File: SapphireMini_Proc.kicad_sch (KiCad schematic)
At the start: 64 parts, among them J801 USB_B_Micro, J802 Conn_02x05_Odd_Even, J803 Conn_02x05_Odd_Even, J805 Conn_01x04_Male, SW801 EVQP7C01P, U801 ATSAMD21G18A-A

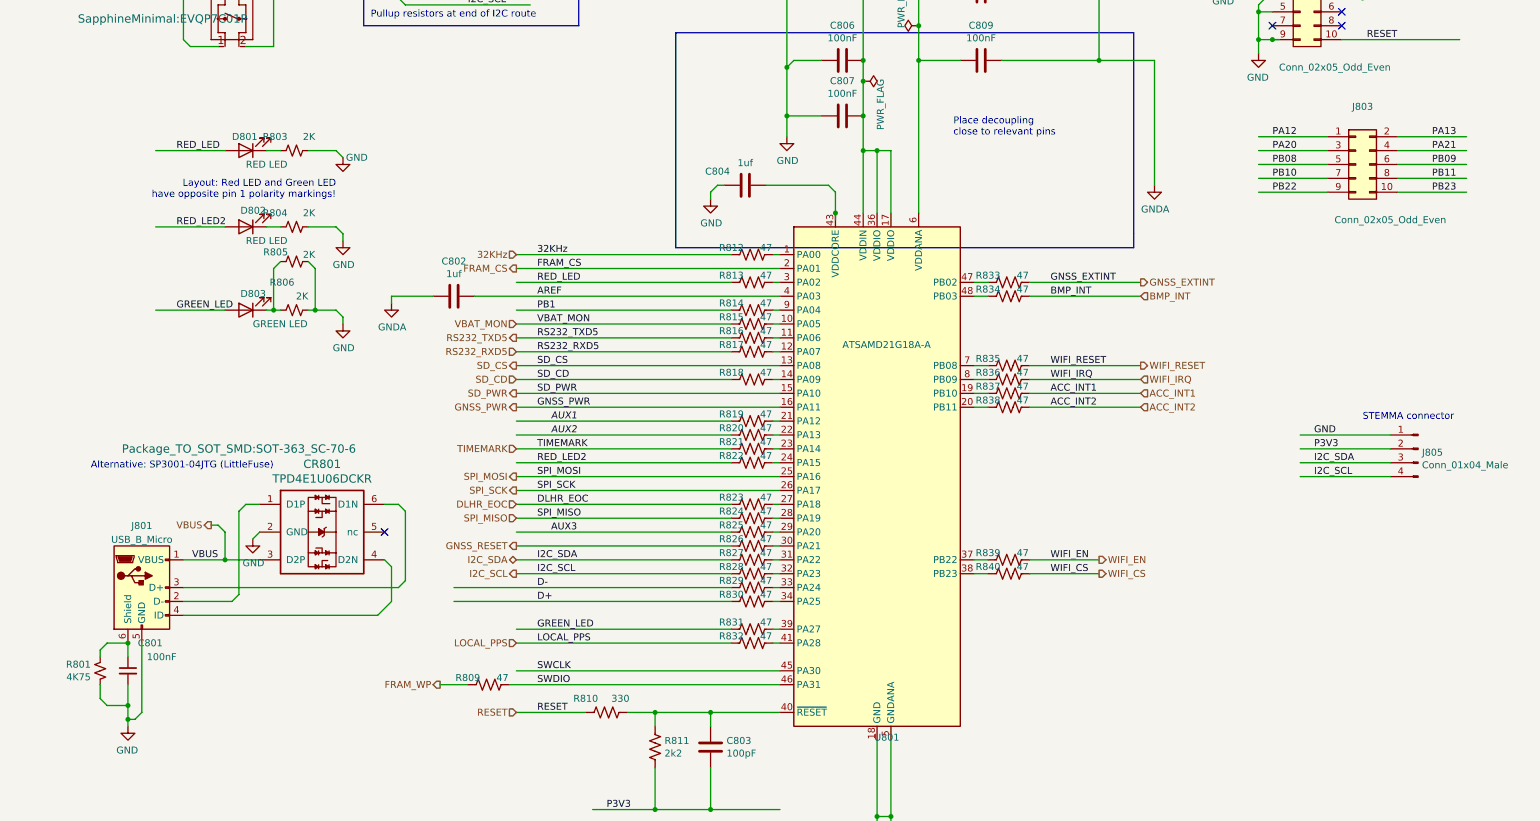
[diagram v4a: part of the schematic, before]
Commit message: replacing w/ resistor array
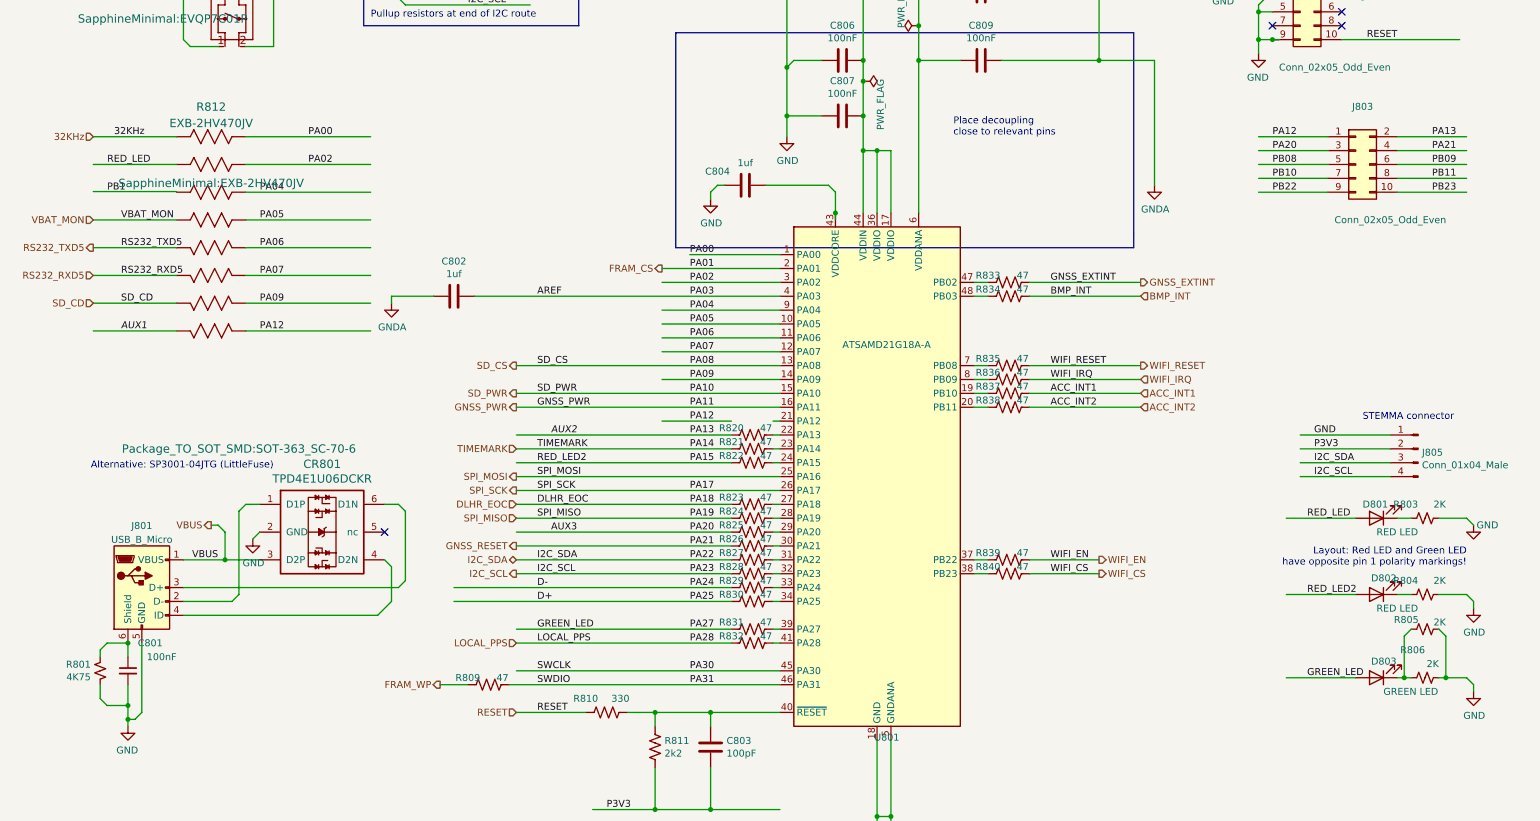
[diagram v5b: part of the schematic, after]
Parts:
- removed R812, R813, R814, R815, R816, R817, R818, R819: 47, Resistor_SMD:R_0603_1608Metric, symbol Device:R_US
- added R812: EXB-2HV470JV, SapphineMinimal:EXB-2HV470JV, symbol PanasonicRA:EXB-2HV470JV
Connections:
- net PA13 is gone; now on net AUX2: J803.2 (Pin_2)
- net PA20 is gone; now on net AUX3: J803.3 (Pin_3)
- net PA21 is gone; now on net GNSS_RESET: J803.4 (Pin_4)
- net 32KHz: now also R812.1
- net AUX1: now also R812.8
- net PA12: now also R812.9
- net RED_LED: now also R812.2
- net RS232_RXD5: now also R812.6
- net RS232_TXD5: now also R812.5
- net SD_CD: now also R812.7
- net VBAT_MON: now also R812.4
- net PA04: now reaches U801.9 (PA04)
- net PA04: now also R812.14
- net PA09: now reaches U801.14 (PA09)
- net PA09: now also R812.10
- net PA05: now reaches U801.10 (PA05)
- net PA05: now also R812.13
- net PA06: now reaches U801.11 (PA06)
- net PA06: now also R812.12
- net PA07: now reaches U801.12 (PA07)
- net PA07: now also R812.11
- net PA02: now reaches U801.3 (PA02)
- net PA02: now also R812.15
- net PA00: now reaches U801.1 (PA00)
- net PA00: now also R812.16
- net RED_LED2 renamed PA15
- net SWCLK renamed PA30
- net SWDIO renamed PA31
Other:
- moved on the sheet: D801, D802, D803, R803, R804, R805, R806

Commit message: Working on update to power controllers
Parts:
- removed R809, R820, R821, R822, R823, R824, R825, R826, R827, R828, R829, R830, R831, R832, R833, R834, R835, R836, R837, R838, R839, R840: 47, Resistor_SMD:R_0603_1608Metric, symbol Device:R_US
- added R809, R813, R814: EXB-2HV470JV, Sapphire:EXB-2HV470JV, symbol PanasonicRA:EXB-2HV470JV
- R812: footprint SapphineMinimal:EXB-2HV470JV -> Sapphire:EXB-2HV470JV
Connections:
- net ACC_INT1: now also R809.2
- net ACC_INT2: now also R809.3
- net AUX2: now also R809.5; no longer J803.2 (Pin_2)
- net AUX3: now also R813.2; no longer J803.3 (Pin_3)
- net BMP_INT: now also R814.7
- net D-: now also R813.6
- net DLHR_EOC: now also U801.27 (PA18), R809.8, R809.9
- net FRAM_WP: now also R814.5
- net GNSS_EXTINT: now also R814.6
- net GNSS_RESET: now also R813.3; no longer J803.4 (Pin_4)
- net GREEN_LED: now also R814.3
- net I2C_SCL: now also U801.32 (PA23), R813.12, R813.5
- net I2C_SDA: now also U801.31 (PA22), R813.13, R813.4
- net LOCAL_PPS: now also U801.41 (PA28), R814.13, R814.4
- net PA04: now also R812.12; no longer R812.14
- net PA05: now also R812.11; no longer R812.13
- net PA06: now also R812.10; no longer R812.12
- net PA07: now also R812.9; no longer R812.11
- net PA09: now also R809.16; no longer R812.10
- net PA12: now also U801.21 (PA12), R809.13; no longer R812.9
- net PA15: now also U801.24 (PA15), R809.10; no longer D802.2 (A)
- net PB08: now also R812.14, U801.7 (PB08)
- net PB09: now also R812.13, U801.8 (PB09)
- net PB1: now also R809.1
- net PB10: now also U801.19 (PB10), R809.15
- net PB11: now also U801.20 (PB11), R809.14
- net PB22: now also U801.37 (PB22), R814.16
- net PB23: now also U801.38 (PB23), R814.15
- net SPI_MISO: now also U801.28 (PA19), R813.1, R813.16
- net TIMEMARK: now also U801.23 (PA14), R809.11, R809.6
- net VBAT_MON: now also R809.4; no longer R812.4
- net WIFI_CS: now also R814.2
- net WIFI_EN: now also R814.1
- net WIFI_IRQ: now also R812.4
- net WIFI_RESET: now also R812.3
- net RESET_PIN: now reaches C803.2, R810.1, R811.1, U801.40 (~{RESET})
- net PA24: now reaches U801.33 (PA24)
- net PA24: now also R813.11
- net PA25: now reaches U801.34 (PA25)
- net PA25: now also R813.10
- net PB02: now reaches U801.47 (PB02)
- net PB02: now also R814.11
- net PA13: now reaches U801.22 (PA13)
- net PA13: now also J803.2 (Pin_2), R809.12
- net PA20: now reaches U801.29 (PA20)
- net PA20: now also J803.3 (Pin_3), R813.15
- net PA21: now reaches U801.30 (PA21)
- net PA21: now also J803.4 (Pin_4), R813.14
- net PA27: now reaches U801.39 (PA27)
- net PA27: now also R814.14
- net PB03: now reaches U801.48 (PB03)
- net PB03: now also R814.10
- net PA30 renamed SWCLK
- net PA31 renamed SWDIO
- net SWDIO: now also R814.12
- new net RED_LED2: D802.2 (A), R809.7
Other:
- company: (none) -> Southern Methodist Univ
- title: (none) -> Sapphire Mini M2
- moved on the sheet: C801, C802, CR801, D801, D802, D803, J801, J803, J805, R801, R803, R804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

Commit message: Checkpoint
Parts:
- SW801: footprint SapphineMinimal:EVQP7C01P -> Sapphire:EVQP7C01P
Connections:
- net D+: now also CR801.6 (D1N), J801.3 (D+), R813.7
- net D-: now also CR801.1 (D1P), J801.2 (D-)
- net DLHR_EOC: no longer R809.9, U801.27 (PA18)
- net I2C_SCL: no longer R813.12, U801.32 (PA23)
- net I2C_SDA: no longer R813.13, U801.31 (PA22)
- net LOCAL_PPS: no longer R814.13, U801.41 (PA28)
- net SPI_MISO: no longer R813.16, U801.28 (PA19)
- net TIMEMARK: no longer R809.11, U801.23 (PA14)
- net AREF renamed PA03
- new net PA14: R809.11, U801.23 (PA14)
- new net PA18: R809.9, U801.27 (PA18)
- new net PA19: R813.16, U801.28 (PA19)
- new net PA22: R813.13, U801.31 (PA22)
- new net PA23: R813.12, U801.32 (PA23)
- new net PA28: R814.13, U801.41 (PA28)
- no-connect marks 4 -> 8
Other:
- note added: "AREF"
- note added: "PA01"
- note added: "PA08"
- note added: "PA10"
- note added: "PA11"
